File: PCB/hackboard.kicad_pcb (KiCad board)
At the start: 2 copper layers, 355.7 x 131.8 mm, 175 parts

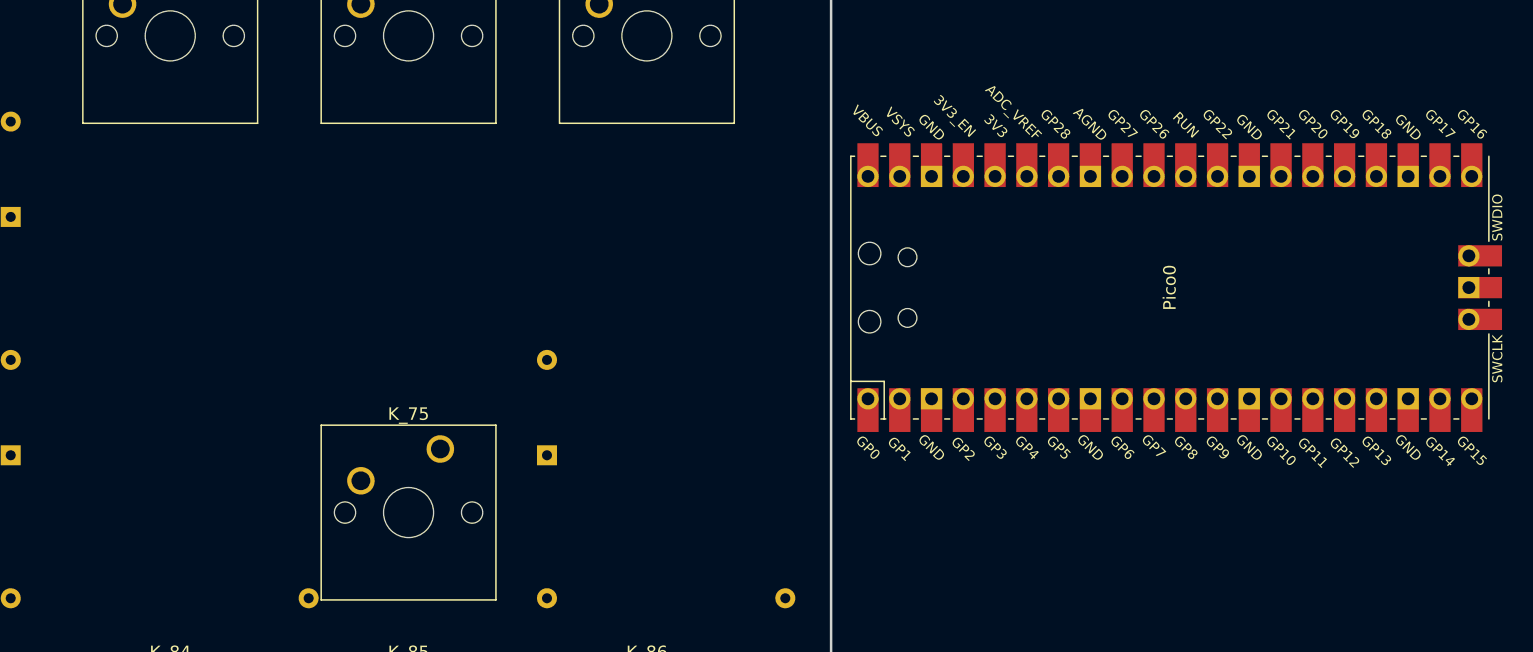
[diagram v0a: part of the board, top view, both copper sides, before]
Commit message: Moved MCB
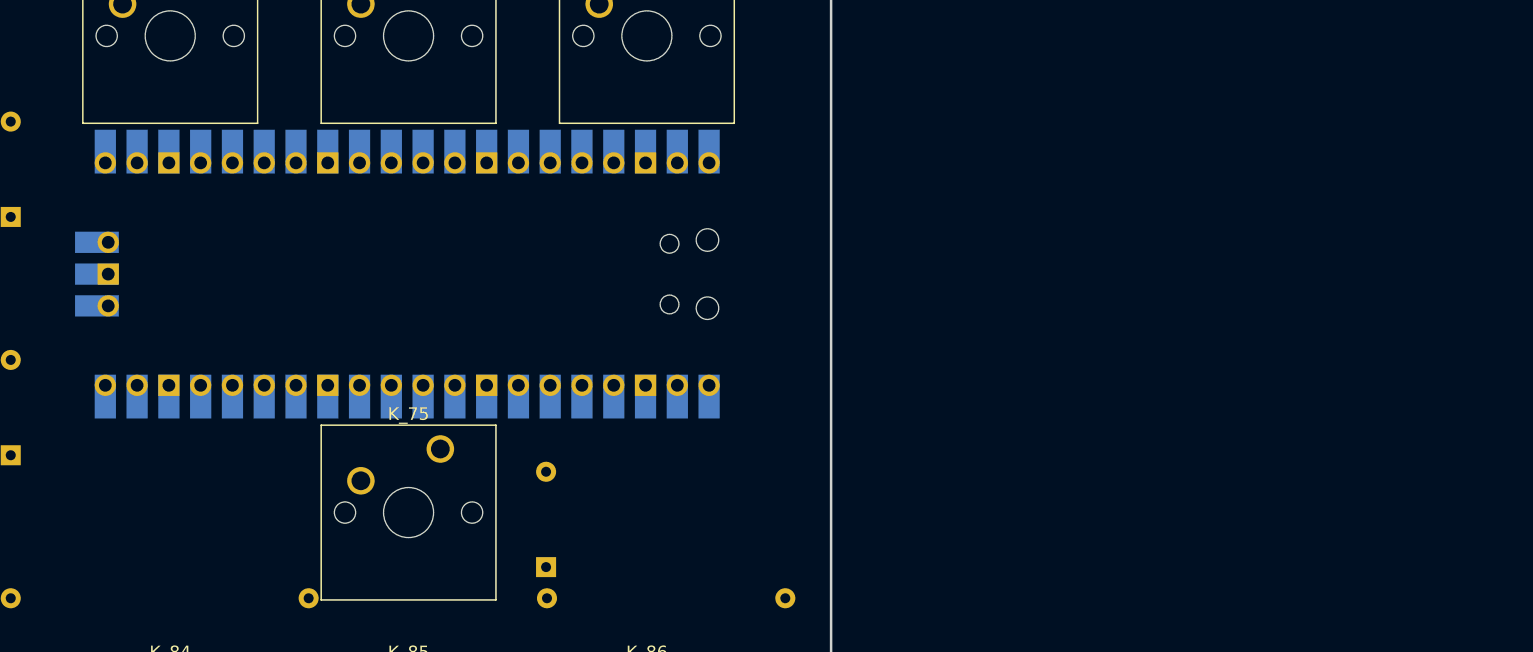
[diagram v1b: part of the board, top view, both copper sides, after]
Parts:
- Pico0: moved to B.Cu
- moved Pico0 61.0 mm to (370.6, 155.3)
- moved D_75 8.94 mm to (381.7, 178.8)

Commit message: Finished Routing
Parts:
- moved Pico0 7.80 mm to (378.4, 155.3)
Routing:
- net row0: track 0.00 -> 422.8 mm
- net col0: track 0.00 -> 422.8 mm, vias 0 -> 1
- net row2: track 0.00 -> 402.5 mm
- net col1: track 0.00 -> 387.9 mm, vias 0 -> 2
- net col2: track 0.00 -> 380.8 mm, vias 0 -> 2
- net col3: track 0.00 -> 379.6 mm, vias 0 -> 1
- net row3: track 0.00 -> 372.1 mm
- net row6: track 0.00 -> 363.4 mm
- net col4: track 0.00 -> 332.8 mm, vias 0 -> 1
- net row5: track 0.00 -> 323.1 mm
- net row4: track 0.00 -> 320.7 mm
- net col5: track 0.00 -> 304.4 mm, vias 0 -> 2
- net col6: track 0.00 -> 284.9 mm, vias 0 -> 2
- net col7: track 0.00 -> 266.2 mm, vias 0 -> 2
- net col8: track 0.00 -> 251.4 mm, vias 0 -> 1
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
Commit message: Moved diodes
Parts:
- moved D_0 3.68 mm to (72.2, 87.8)
- moved D_1 3.68 mm to (110.3, 87.8)
- moved D_10 3.68 mm to (300.8, 87.8)
- moved D_11 3.68 mm to (319.8, 87.8)
- moved D_12 3.68 mm to (338.9, 87.8)
- moved D_13 3.68 mm to (362.7, 87.8)
- moved D_14 3.68 mm to (381.7, 87.8)
- moved D_15 3.68 mm to (400.8, 87.8)
- moved D_2 3.68 mm to (129.3, 87.8)
- moved D_3 3.68 mm to (148.4, 87.8)
- moved D_4 3.68 mm to (167.4, 87.8)
- moved D_5 3.68 mm to (196.0, 87.8)
- moved D_6 3.68 mm to (215.0, 87.8)
- moved D_7 3.68 mm to (234.1, 87.8)
- moved D_8 3.68 mm to (253.1, 87.8)
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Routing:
- net row0: track 422.8 -> 460.9 mm
- net col0: track 422.8 -> 439.0 mm
- net col17: track 131.4 -> 116.7 mm
- net col6: track 284.9 -> 275.5 mm, vias 2 -> 1
- net col2: track 380.8 -> 389.8 mm, vias 2 -> 3
- net row2: track 402.5 -> 395.8 mm
- net col13: track 176.6 -> 183.0 mm, vias 1 -> 2
- net Net-(D_85-A): track 18.9 -> 24.5 mm, vias 0 -> 1
- net col8: track 251.4 -> 256.6 mm
- net Net-(D_49-A): track 23.8 -> 19.5 mm, vias 1 -> 0
- net col3: track 379.6 -> 383.8 mm, vias 1 -> 3
- net col7: track 266.2 -> 262.1 mm
- net col14: track 154.6 -> 158.7 mm
- net row5: track 323.1 -> 319.3 mm
- net Net-(D_23-A): track 18.9 -> 22.5 mm, vias 0 -> 1
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
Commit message: Updated symbols and routing
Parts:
- added G***: LOGO, LOGO, B.Cu at (185.5, 168.8)
- D_0, D_1, D_10, D_11, D_12, D_13, D_14, D_15, D_16, D_17, D_18, D_19, D_2, D_20, D_21, D_22, D_23, D_24, D_25, D_26, D_27, D_28, D_29, D_3, D_30, D_31, D_32, D_33, D_34, D_35, D_36, D_37, D_38, D_39, D_4, D_40, D_41, D_42, D_43, D_44, D_45, D_46, D_47, D_48, D_49, D_5, D_50, D_51, D_52, D_53, D_54, D_55, D_56, D_57, D_58, D_59, D_6, D_60, D_61, D_62, D_63, D_64, D_65, D_66, D_67, D_68, D_69, D_7, D_70, D_71, D_72, D_73, D_74, D_75, D_76, D_77, D_78, D_79, D_8, D_80, D_81, D_82, D_83, D_84, D_85, D_86, D_9: value D -> 1N4148
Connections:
- K_0 pad 1: col0 -> Net-(D_0-A)
- K_0 pad 2: Net-(D_0-A) -> col0
- K_1 pad 1: col2 -> Net-(D_1-A)
- K_1 pad 2: Net-(D_1-A) -> col2
- K_10 pad 1: col12 -> Net-(D_10-A)
- K_10 pad 2: Net-(D_10-A) -> col12
- K_11 pad 1: col13 -> Net-(D_11-A)
- K_11 pad 2: Net-(D_11-A) -> col13
- K_12 pad 1: col14 -> Net-(D_12-A)
- K_12 pad 2: Net-(D_12-A) -> col14
- K_13 pad 1: col15 -> Net-(D_13-A)
- K_13 pad 2: Net-(D_13-A) -> col15
- K_14 pad 1: col16 -> Net-(D_14-A)
- K_14 pad 2: Net-(D_14-A) -> col16
- K_15 pad 1: col17 -> Net-(D_15-A)
- K_15 pad 2: Net-(D_15-A) -> col17
- K_16 pad 1: col0 -> Net-(D_16-A)
- K_16 pad 2: Net-(D_16-A) -> col0
- K_17 pad 1: col1 -> Net-(D_17-A)
- K_17 pad 2: Net-(D_17-A) -> col1
- K_18 pad 1: col2 -> Net-(D_18-A)
- K_18 pad 2: Net-(D_18-A) -> col2
- K_19 pad 1: col3 -> Net-(D_19-A)
- K_19 pad 2: Net-(D_19-A) -> col3
- K_2 pad 1: col3 -> Net-(D_2-A)
- K_2 pad 2: Net-(D_2-A) -> col3
- K_20 pad 1: col4 -> Net-(D_20-A)
- K_20 pad 2: Net-(D_20-A) -> col4
- K_21 pad 1: col5 -> Net-(D_21-A)
- K_21 pad 2: Net-(D_21-A) -> col5
- K_22 pad 1: col6 -> Net-(D_22-A)
- K_22 pad 2: Net-(D_22-A) -> col6
- K_23 pad 1: col7 -> Net-(D_23-A)
- K_23 pad 2: Net-(D_23-A) -> col7
- K_24 pad 1: col8 -> Net-(D_24-A)
- K_24 pad 2: Net-(D_24-A) -> col8
- K_25 pad 1: col9 -> Net-(D_25-A)
- K_25 pad 2: Net-(D_25-A) -> col9
- K_26 pad 1: col10 -> Net-(D_26-A)
- K_26 pad 2: Net-(D_26-A) -> col10
- K_27 pad 1: col11 -> Net-(D_27-A)
- K_27 pad 2: Net-(D_27-A) -> col11
- K_28 pad 1: col12 -> Net-(D_28-A)
- K_28 pad 2: Net-(D_28-A) -> col12
- K_29 pad 1: col14 -> Net-(D_29-A)
- K_29 pad 2: Net-(D_29-A) -> col14
- K_3 pad 1: col4 -> Net-(D_3-A)
- K_3 pad 2: Net-(D_3-A) -> col4
- K_30 pad 1: col15 -> Net-(D_30-A)
- K_30 pad 2: Net-(D_30-A) -> col15
- K_31 pad 1: col16 -> Net-(D_31-A)
- K_31 pad 2: Net-(D_31-A) -> col16
- K_32 pad 1: col17 -> Net-(D_32-A)
- K_32 pad 2: Net-(D_32-A) -> col17
- K_33 pad 1: col0 -> Net-(D_33-A)
- K_33 pad 2: Net-(D_33-A) -> col0
- K_34 pad 1: col2 -> Net-(D_34-A)
- K_34 pad 2: Net-(D_34-A) -> col2
- K_35 pad 1: col3 -> Net-(D_35-A)
- K_35 pad 2: Net-(D_35-A) -> col3
- K_36 pad 1: col4 -> Net-(D_36-A)
- K_36 pad 2: Net-(D_36-A) -> col4
- K_37 pad 1: col5 -> Net-(D_37-A)
- K_37 pad 2: Net-(D_37-A) -> col5
- K_38 pad 1: col6 -> Net-(D_38-A)
- K_38 pad 2: Net-(D_38-A) -> col6
- K_39 pad 1: col7 -> Net-(D_39-A)
- K_39 pad 2: Net-(D_39-A) -> col7
- K_4 pad 1: col5 -> Net-(D_4-A)
- K_4 pad 2: Net-(D_4-A) -> col5
- K_40 pad 1: col8 -> Net-(D_40-A)
- K_40 pad 2: Net-(D_40-A) -> col8
- K_41 pad 1: col9 -> Net-(D_41-A)
- K_41 pad 2: Net-(D_41-A) -> col9
- K_42 pad 1: col10 -> Net-(D_42-A)
- K_42 pad 2: Net-(D_42-A) -> col10
- K_43 pad 1: col11 -> Net-(D_43-A)
- K_43 pad 2: Net-(D_43-A) -> col11
- K_44 pad 1: col12 -> Net-(D_44-A)
- K_44 pad 2: Net-(D_44-A) -> col12
- K_45 pad 1: col13 -> Net-(D_45-A)
- K_45 pad 2: Net-(D_45-A) -> col13
- K_46 pad 1: col14 -> Net-(D_46-A)
- K_46 pad 2: Net-(D_46-A) -> col14
- K_47 pad 1: col15 -> Net-(D_47-A)
- K_47 pad 2: Net-(D_47-A) -> col15
- K_48 pad 1: col16 -> Net-(D_48-A)
- K_48 pad 2: Net-(D_48-A) -> col16
- K_49 pad 1: col17 -> Net-(D_49-A)
- K_49 pad 2: Net-(D_49-A) -> col17
- K_5 pad 1: col7 -> Net-(D_5-A)
- K_5 pad 2: Net-(D_5-A) -> col7
- K_50 pad 1: col0 -> Net-(D_50-A)
- K_50 pad 2: Net-(D_50-A) -> col0
- K_51 pad 1: col2 -> Net-(D_51-A)
- K_51 pad 2: Net-(D_51-A) -> col2
- K_52 pad 1: col3 -> Net-(D_52-A)
- K_52 pad 2: Net-(D_52-A) -> col3
- K_53 pad 1: col4 -> Net-(D_53-A)
- K_53 pad 2: Net-(D_53-A) -> col4
- K_54 pad 1: col5 -> Net-(D_54-A)
- K_54 pad 2: Net-(D_54-A) -> col5
- K_55 pad 1: col6 -> Net-(D_55-A)
- K_55 pad 2: Net-(D_55-A) -> col6
- K_56 pad 1: col7 -> Net-(D_56-A)
- K_56 pad 2: Net-(D_56-A) -> col7
- K_57 pad 1: col8 -> Net-(D_57-A)
- K_57 pad 2: Net-(D_57-A) -> col8
- K_58 pad 1: col9 -> Net-(D_58-A)
- K_58 pad 2: Net-(D_58-A) -> col9
- K_59 pad 1: col10 -> Net-(D_59-A)
- K_59 pad 2: Net-(D_59-A) -> col10
- K_6 pad 1: col8 -> Net-(D_6-A)
- K_6 pad 2: Net-(D_6-A) -> col8
- K_60 pad 1: col11 -> Net-(D_60-A)
- K_60 pad 2: Net-(D_60-A) -> col11
- K_61 pad 1: col12 -> Net-(D_61-A)
- K_61 pad 2: Net-(D_61-A) -> col12
- K_62 pad 1: col13 -> Net-(D_62-A)
- K_62 pad 2: Net-(D_62-A) -> col13
- K_63 pad 1: col1 -> Net-(D_63-A)
- K_63 pad 2: Net-(D_63-A) -> col1
- K_64 pad 1: col2 -> Net-(D_64-A)
- K_64 pad 2: Net-(D_64-A) -> col2
- K_65 pad 1: col3 -> Net-(D_65-A)
- K_65 pad 2: Net-(D_65-A) -> col3
- K_66 pad 1: col4 -> Net-(D_66-A)
- K_66 pad 2: Net-(D_66-A) -> col4
- K_67 pad 1: col5 -> Net-(D_67-A)
- K_67 pad 2: Net-(D_67-A) -> col5
- K_68 pad 1: col6 -> Net-(D_68-A)
- K_68 pad 2: Net-(D_68-A) -> col6
- K_69 pad 1: col7 -> Net-(D_69-A)
- K_69 pad 2: Net-(D_69-A) -> col7
- K_7 pad 1: col9 -> Net-(D_7-A)
- K_7 pad 2: Net-(D_7-A) -> col9
- K_70 pad 1: col8 -> Net-(D_70-A)
- K_70 pad 2: Net-(D_70-A) -> col8
- K_71 pad 1: col9 -> Net-(D_71-A)
- K_71 pad 2: Net-(D_71-A) -> col9
- K_72 pad 1: col10 -> Net-(D_72-A)
- K_72 pad 2: Net-(D_72-A) -> col10
- K_73 pad 1: col11 -> Net-(D_73-A)
- K_73 pad 2: Net-(D_73-A) -> col11
- K_74 pad 1: col13 -> Net-(D_74-A)
- K_74 pad 2: Net-(D_74-A) -> col13
- K_75 pad 1: col16 -> Net-(D_75-A)
- K_75 pad 2: Net-(D_75-A) -> col16
- K_76 pad 1: col0 -> Net-(D_76-A)
- K_76 pad 2: Net-(D_76-A) -> col0
- K_77 pad 1: col1 -> Net-(D_77-A)
- K_77 pad 2: Net-(D_77-A) -> col1
- K_78 pad 1: col3 -> Net-(D_78-A)
- K_78 pad 2: Net-(D_78-A) -> col3
- K_79 pad 1: col6 -> Net-(D_79-A)
- K_79 pad 2: Net-(D_79-A) -> col6
- K_8 pad 1: col10 -> Net-(D_8-A)
- K_8 pad 2: Net-(D_8-A) -> col10
- K_80 pad 1: col10 -> Net-(D_80-A)
- K_80 pad 2: Net-(D_80-A) -> col10
- K_81 pad 1: col11 -> Net-(D_81-A)
- K_81 pad 2: Net-(D_81-A) -> col11
- K_82 pad 1: col13 -> Net-(D_82-A)
- K_82 pad 2: Net-(D_82-A) -> col13
- K_83 pad 1: col14 -> Net-(D_83-A)
- K_83 pad 2: Net-(D_83-A) -> col14
- K_84 pad 1: col15 -> Net-(D_84-A)
- K_84 pad 2: Net-(D_84-A) -> col15
- K_85 pad 1: col16 -> Net-(D_85-A)
- K_85 pad 2: Net-(D_85-A) -> col16
- K_86 pad 1: col17 -> Net-(D_86-A)
- K_86 pad 2: Net-(D_86-A) -> col17
- K_9 pad 1: col11 -> Net-(D_9-A)
- K_9 pad 2: Net-(D_9-A) -> col11
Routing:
- net col13: track 183.0 -> 197.3 mm, vias 2 -> 0
- net Net-(D_51-A): track 25.3 -> 11.5 mm, vias 1 -> 0
- net Net-(D_32-A): track 24.5 -> 11.5 mm, vias 1 -> 0
- net Net-(D_28-A): track 24.5 -> 11.5 mm, vias 1 -> 0
- net Net-(D_20-A): track 24.5 -> 11.5 mm, vias 1 -> 0
- net Net-(D_58-A): track 24.5 -> 11.5 mm, vias 1 -> 0
- net Net-(D_55-A): track 24.5 -> 11.5 mm, vias 1 -> 0
- net Net-(D_18-A): track 24.5 -> 11.5 mm, vias 1 -> 0
- net Net-(D_72-A): track 24.5 -> 11.5 mm, vias 1 -> 0
- net Net-(D_30-A): track 24.5 -> 11.5 mm, vias 1 -> 0
- net Net-(D_85-A): track 24.5 -> 11.5 mm, vias 1 -> 0
- net Net-(D_48-A): track 24.5 -> 11.5 mm, vias 1 -> 0
- net col8: track 256.6 -> 244.4 mm
- net Net-(D_19-A): track 23.4 -> 11.5 mm, vias 1 -> 0
- net Net-(D_21-A): track 23.2 -> 11.5 mm, vias 1 -> 0
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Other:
- board size 355.7 x 131.8 mm -> 355.7 x 129.3 mm

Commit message: Removed unused row
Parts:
- moved G*** 5.61 mm to (184.5, 163.3)
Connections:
- D_16 pad 1: row2 -> row1
- D_17 pad 1: row2 -> row1
- D_18 pad 1: row2 -> row1
- D_19 pad 1: row2 -> row1
- D_20 pad 1: row2 -> row1
- D_21 pad 1: row2 -> row1
- D_22 pad 1: row2 -> row1
- D_23 pad 1: row2 -> row1
- D_24 pad 1: row2 -> row1
- D_25 pad 1: row2 -> row1
- D_26 pad 1: row2 -> row1
- D_27 pad 1: row2 -> row1
- D_28 pad 1: row2 -> row1
- D_29 pad 1: row2 -> row1
- D_30 pad 1: row2 -> row1
- D_31 pad 1: row2 -> row1
- D_32 pad 1: row2 -> row1
- D_33 pad 1: row3 -> row2
- D_34 pad 1: row3 -> row2
- D_35 pad 1: row3 -> row2
- D_36 pad 1: row3 -> row2
- D_37 pad 1: row3 -> row2
- D_38 pad 1: row3 -> row2
- D_39 pad 1: row3 -> row2
- D_40 pad 1: row3 -> row2
- D_41 pad 1: row3 -> row2
- D_42 pad 1: row3 -> row2
- D_43 pad 1: row3 -> row2
- D_44 pad 1: row3 -> row2
- D_45 pad 1: row3 -> row2
- D_46 pad 1: row3 -> row2
- D_47 pad 1: row3 -> row2
- D_48 pad 1: row3 -> row2
- D_49 pad 1: row3 -> row2
- D_50 pad 1: row4 -> row3
- D_51 pad 1: row4 -> row3
- D_52 pad 1: row4 -> row3
- D_53 pad 1: row4 -> row3
- D_54 pad 1: row4 -> row3
- D_55 pad 1: row4 -> row3
- D_56 pad 1: row4 -> row3
- D_57 pad 1: row4 -> row3
- D_58 pad 1: row4 -> row3
- D_59 pad 1: row4 -> row3
- D_60 pad 1: row4 -> row3
- D_61 pad 1: row4 -> row3
- D_62 pad 1: row4 -> row3
- D_63 pad 1: row5 -> row4
- D_64 pad 1: row5 -> row4
- D_65 pad 1: row5 -> row4
- D_66 pad 1: row5 -> row4
- D_67 pad 1: row5 -> row4
- D_68 pad 1: row5 -> row4
- D_69 pad 1: row5 -> row4
- D_70 pad 1: row5 -> row4
- D_71 pad 1: row5 -> row4
- D_72 pad 1: row5 -> row4
- D_73 pad 1: row5 -> row4
- D_74 pad 1: row5 -> row4
- D_75 pad 1: row5 -> row4
- D_76 pad 1: row6 -> row5
- D_77 pad 1: row6 -> row5
- D_78 pad 1: row6 -> row5
- D_79 pad 1: row6 -> row5
- D_80 pad 1: row6 -> row5
- D_81 pad 1: row6 -> row5
- D_82 pad 1: row6 -> row5
- D_83 pad 1: row6 -> row5
- D_84 pad 1: row6 -> row5
- D_85 pad 1: row6 -> row5
- D_86 pad 1: row6 -> row5
- Pico0 pad 10: col0 -> col1
- Pico0 pad 11: col1 -> col2
- Pico0 pad 12: col2 -> col3
- Pico0 pad 13: unconnected-(Pico0-GND-Pad13) -> GND
- Pico0 pad 14: col3 -> col4
- Pico0 pad 15: col4 -> col5
- Pico0 pad 16: col5 -> col6
- Pico0 pad 17: col6 -> col7
- Pico0 pad 18: unconnected-(Pico0-GND-Pad18) -> GND
- Pico0 pad 19: col7 -> col8
- Pico0 pad 20: col8 -> col9
- Pico0 pad 21: col9 -> col10
- Pico0 pad 22: col10 -> col11
- Pico0 pad 23: unconnected-(Pico0-GND-Pad23) -> GND
- Pico0 pad 24: col11 -> col12
- Pico0 pad 25: col12 -> col13
- Pico0 pad 26: col13 -> col14
- Pico0 pad 27: col14 -> col15
- Pico0 pad 28: unconnected-(Pico0-GND-Pad28) -> GND
- Pico0 pad 29: col15 -> col16
- Pico0 pad 3: unconnected-(Pico0-GND-Pad3) -> GND
- Pico0 pad 31: col16 -> col17
- Pico0 pad 32: col17 -> unconnected-(Pico0-GPIO27_ADC1-Pad32)
- Pico0 pad 38: unconnected-(Pico0-GND-Pad38) -> GND
- Pico0 pad 8: unconnected-(Pico0-GND-Pad8) -> GND
- Pico0 pad 9: row6 -> col0
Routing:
- net row1: track 0.00 -> 400.7 mm
- net row6: track 360.5 -> 0.00 mm, vias 1 -> 0
- net GND: track 0.00 -> 96.2 mm
- net row3: track 368.1 -> 323.2 mm, vias 0 -> 2
- net row5: track 320.0 -> 359.9 mm
- net row2: track 402.8 -> 367.0 mm
- net col0: track 431.1 -> 446.7 mm, vias 0 -> 2
- net col9: track 238.1 -> 226.0 mm, vias 0 -> 1
- net col6: track 278.3 -> 288.9 mm
- net col11: track 220.3 -> 211.7 mm, vias 0 -> 1
- net col1: track 400.4 -> 392.7 mm
- net col7: track 267.0 -> 272.9 mm
- net col4: track 339.5 -> 333.9 mm
- net col15: track 135.0 -> 129.8 mm
- net col8: track 244.4 -> 249.6 mm
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
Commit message: Changed silkscreen art
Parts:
- moved G*** 134.1 mm to (318.6, 161.5)
- moved Pico0 1.52 mm to (378.4, 153.8)
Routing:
- net row3: track 323.2 -> 340.1 mm, vias 2 -> 4
- net col0: track 446.7 -> 433.3 mm, vias 2 -> 0
- net col7: track 272.9 -> 286.0 mm
- net col1: track 392.7 -> 401.2 mm
- net col5: track 314.9 -> 310.5 mm, vias 2 -> 1
- net col14: track 160.9 -> 164.9 mm, vias 1 -> 0
- net col8: track 249.6 -> 245.8 mm
- net col11: track 211.7 -> 215.0 mm, vias 1 -> 0
- net col12: track 157.8 -> 155.0 mm, vias 0 -> 1
- net col3: track 384.4 -> 381.9 mm
- net col2: track 385.8 -> 383.3 mm
- net col9: track 226.0 -> 228.4 mm
- net col6: track 288.9 -> 291.0 mm, vias 1 -> 2
- net row0: track 457.6 -> 456.1 mm
- net row2: track 367.0 -> 365.5 mm
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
